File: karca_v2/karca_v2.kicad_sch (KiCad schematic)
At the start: 4 parts

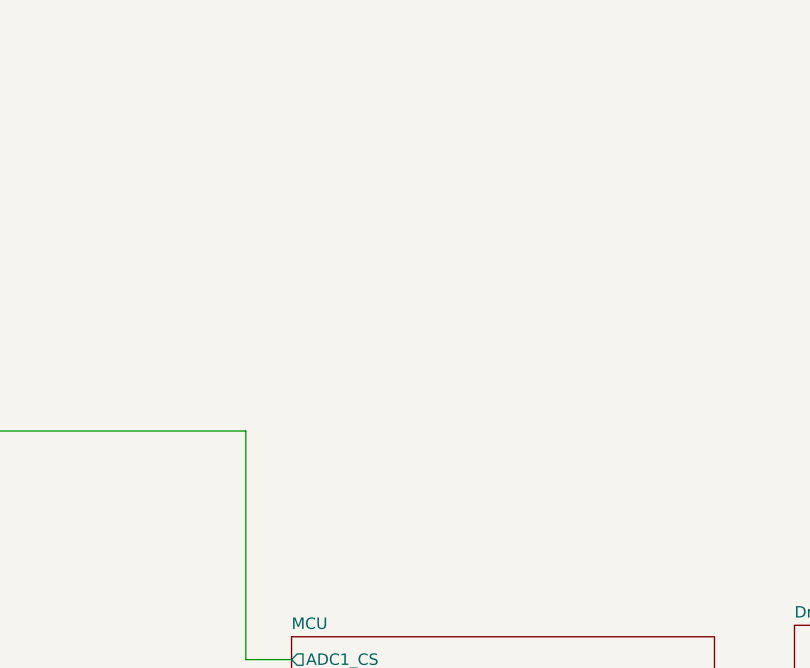
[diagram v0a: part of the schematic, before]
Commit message: finished schematic for v2.1
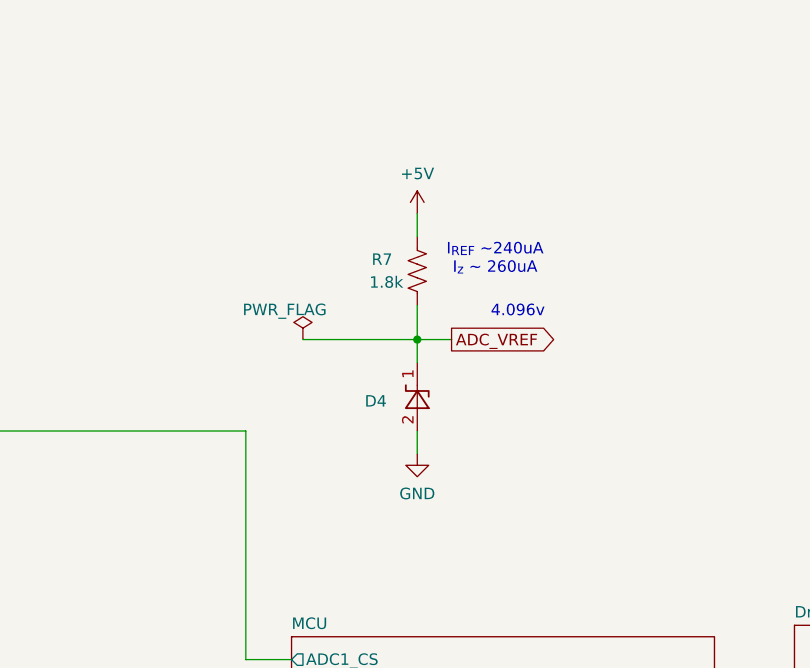
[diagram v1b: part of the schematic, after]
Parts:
- added D4: LM4040DBZ-4.1, Package_TO_SOT_SMD:SOT-23, symbol Reference_Voltage:LM4040DBZ-4.1
- added R7: 1.8k, Resistor_SMD:R_0603_1608Metric, symbol Device:R_US
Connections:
- new net +5V: R7.1
- new net ADC_VREF: D4.1 (K), R7.2
- new net GND: D4.2 (A)
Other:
- note added: "4.096v"
- note added: "I_{REF} ~240uA I_{z} ~ 260uA"

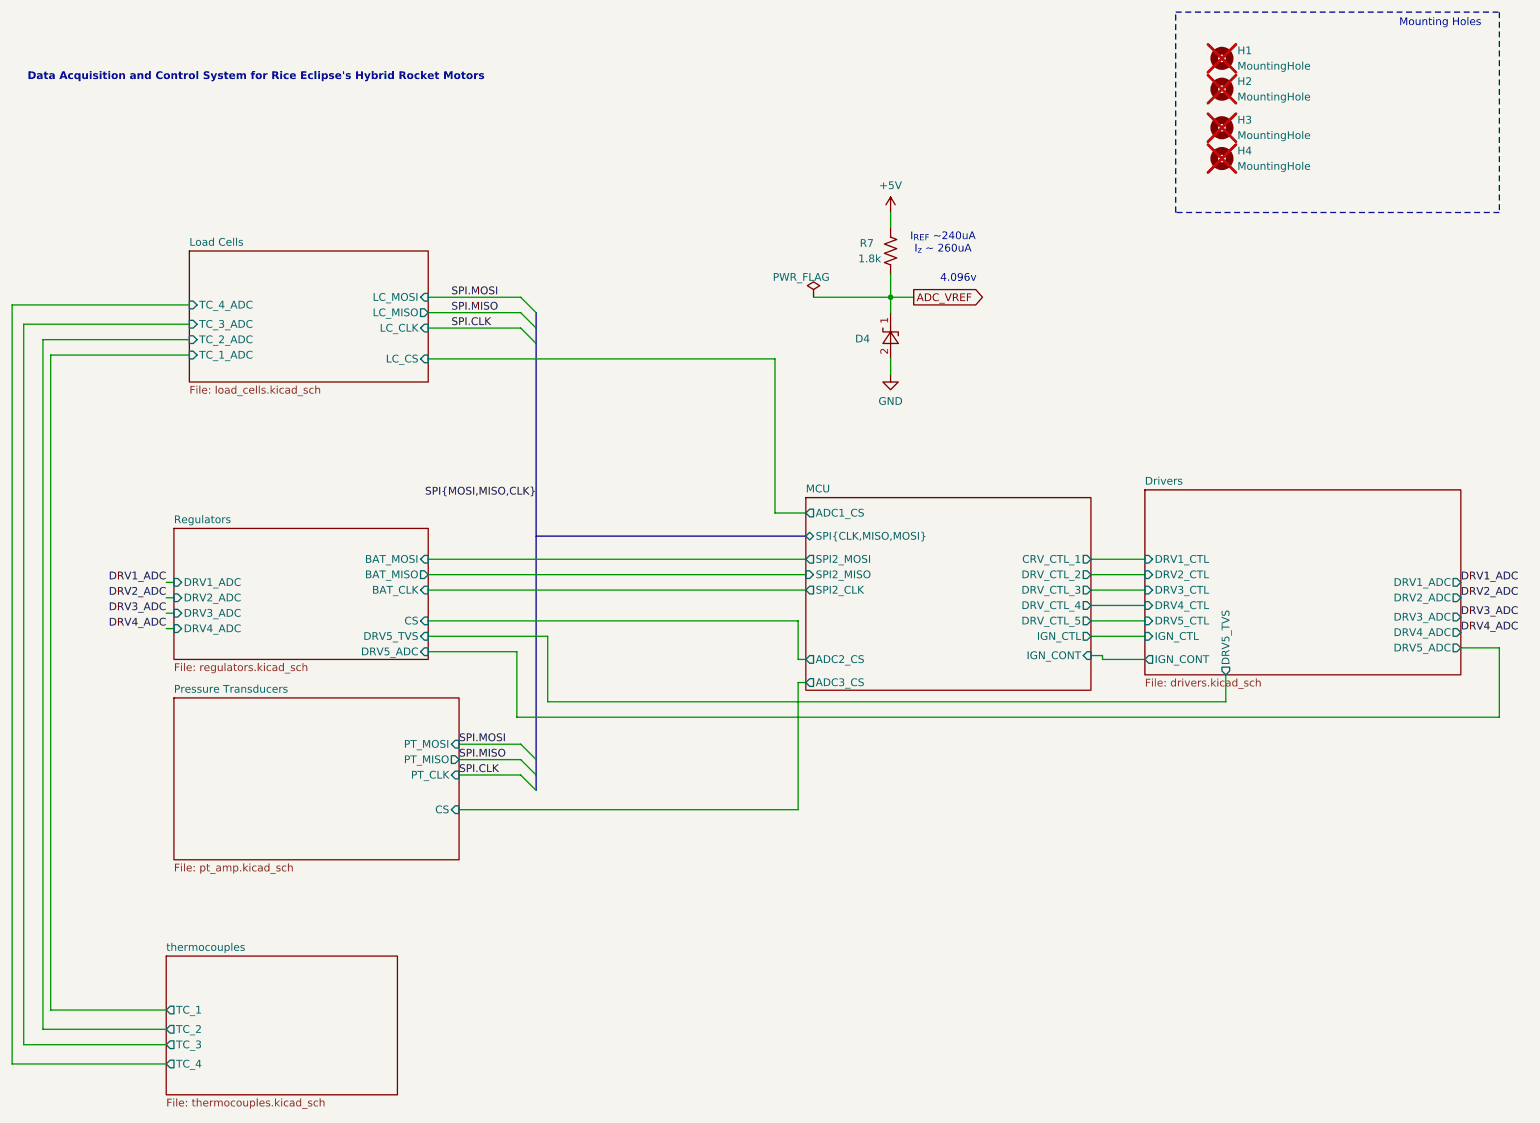
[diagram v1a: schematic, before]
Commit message: swapped adcs
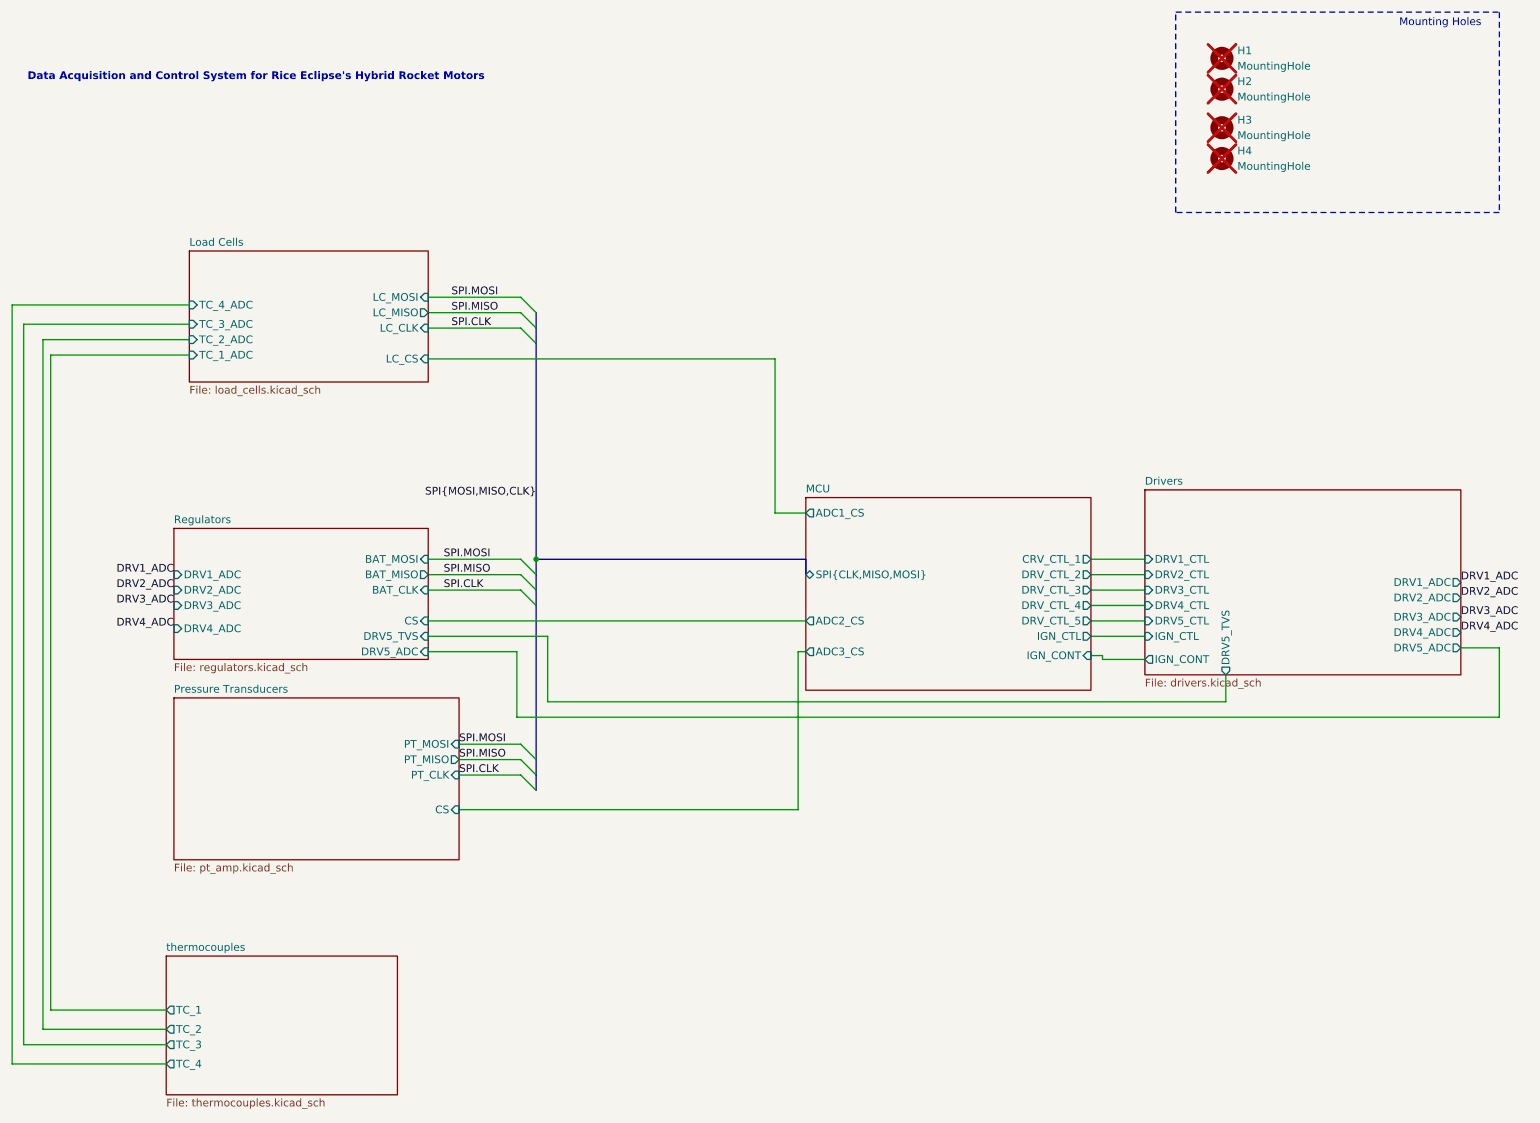
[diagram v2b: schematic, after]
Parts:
- removed D4: LM4040DBZ-4.1, Package_TO_SOT_SMD:SOT-23, symbol Reference_Voltage:LM4040DBZ-4.1
- removed R7: 1.8k, Resistor_SMD:R_0603_1608Metric, symbol Device:R_US
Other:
- sheet MCU ports: added none; removed SPI2_CLK, SPI2_MISO, SPI2_MOSI
- note removed: "4.096v"
- note removed: "I_{REF} ~240uA I_{z} ~ 260uA"

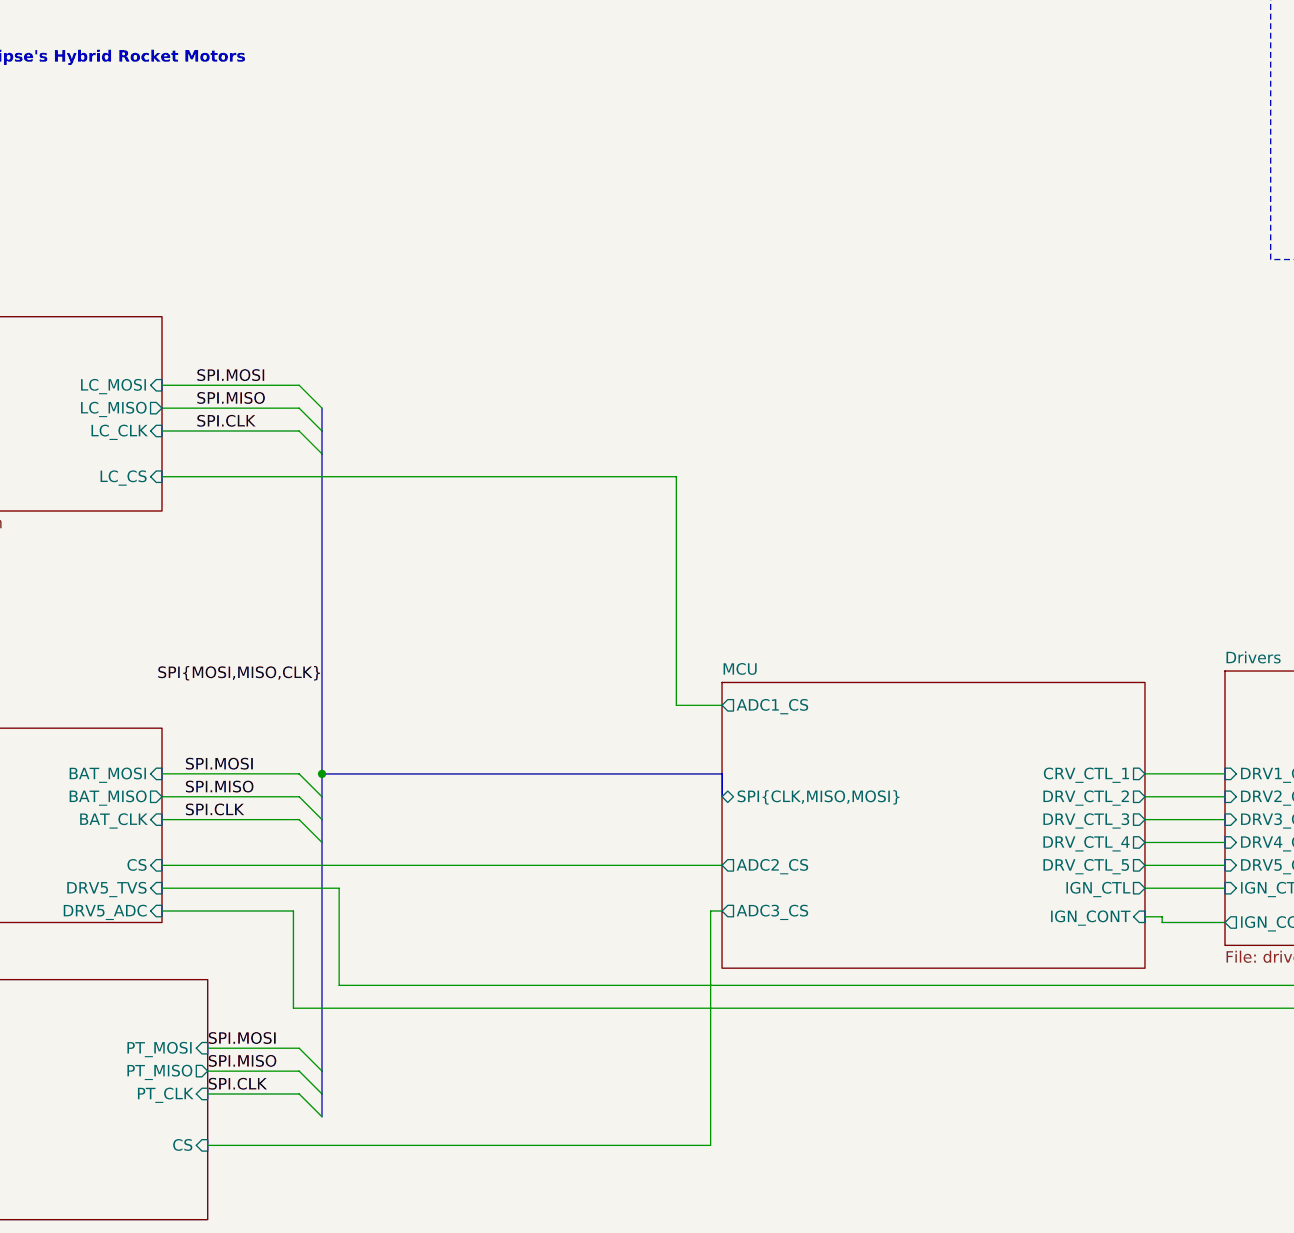
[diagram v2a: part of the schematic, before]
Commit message: added precision shunt reference to ADCs and second SPI bus for driver current and battery voltage monitors
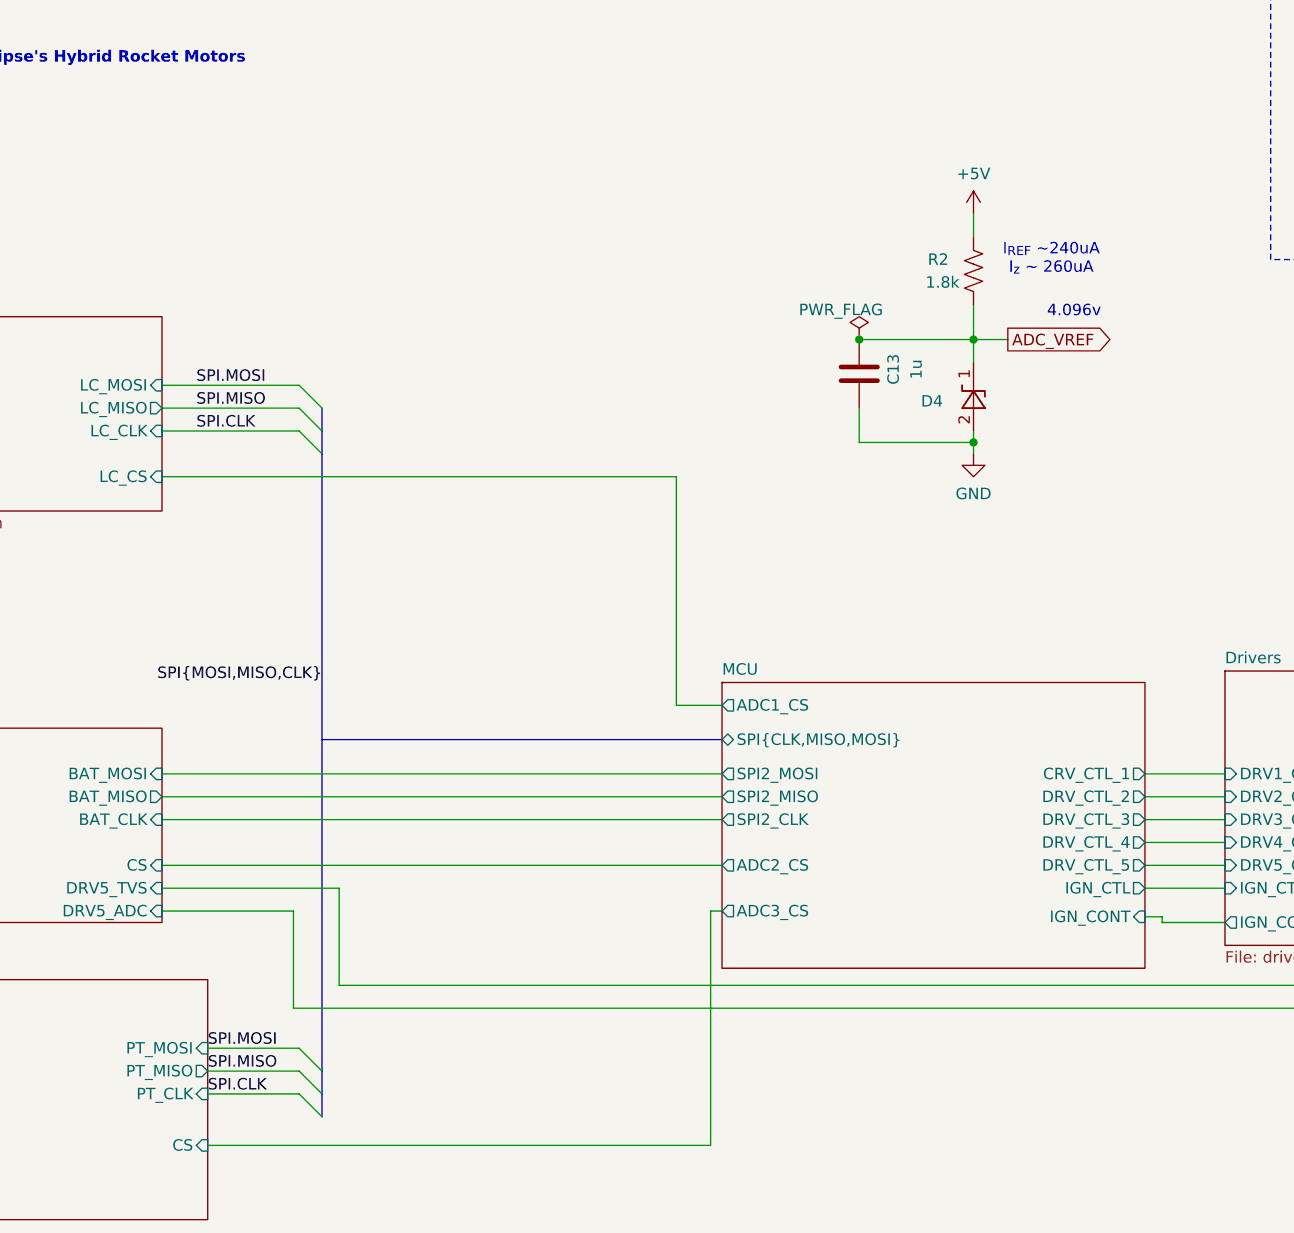
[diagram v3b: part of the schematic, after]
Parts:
- added C13: 1u, Capacitor_SMD:C_0805_2012Metric, symbol Device:C
- added D4: LM4040DBZ-4.1, Package_TO_SOT_SMD:SOT-23, symbol Reference_Voltage:LM4040DBZ-4.1
- added R2: 1.8k, Resistor_SMD:R_0603_1608Metric, symbol Device:R_US
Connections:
- new net +5V: R2.1
- new net ADC_VREF: C13.2, D4.1 (K), R2.2
- new net GND: C13.1, D4.2 (A)
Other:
- sheet MCU ports: added SPI2_CLK, SPI2_MISO, SPI2_MOSI; removed none
- note added: "4.096v"
- note added: "I_{REF} ~240uA I_{z} ~ 260uA"
